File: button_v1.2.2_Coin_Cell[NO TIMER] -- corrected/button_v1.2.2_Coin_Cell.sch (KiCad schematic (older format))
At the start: 20 parts, among them J1 Conn_01x05_Female, SW1 SW_Push, SW2 SW_Push, U1 TPS61097A, X1 ESP-12E

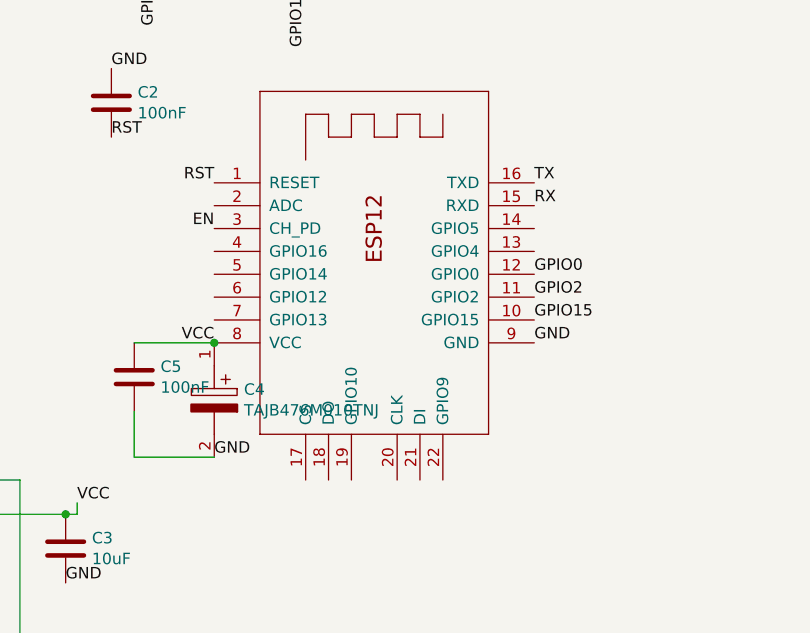
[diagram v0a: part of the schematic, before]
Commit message: All Footprints corrected
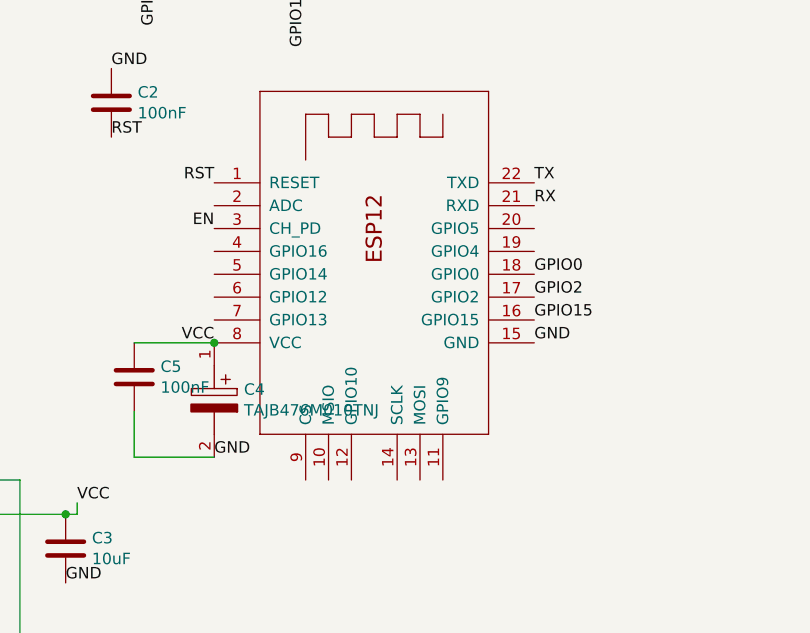
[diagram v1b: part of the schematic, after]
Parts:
- removed X1: ESP-12E, RF_Module:ESP-12E, symbol button_v1.2.2_Coin_Cell-rescue:ESP-12E-ardafruit-button-timer-rescue-button-tim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
- added X1: ESP-12E, handsolder:ESP-12Elesssilk, symbol ardafruit:ESP-12E
- D1: footprint LED_SMD:LED_1206_3216Metric_Castellated -> handsolder:LED_1206_3216Metric_Castellated
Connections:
- net EN: now also X1.3 (CH_PD)
- net GND: now also X1.15 (GND)
- net GPIO0: now also X1.18 (GPIO0)
- net GPIO15: now also X1.16 (GPIO15)
- net GPIO2: now also X1.17 (GPIO2)
- net RST: now also X1.1 (RESET)
- net RX: now also X1.21 (RXD)
- net TX: now also X1.22 (TXD)
- net VCC: now also X1.8 (VCC)
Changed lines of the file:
@@
 F 0 "D1" V 2547 3478 50  0000 L CNN
 F 1 "LED" V 2638 3478 50  0000 L CNN
-F 2 "LED_SMD:LED_1206_3216Metric_Castellated" H 2600 3400 50  0001 C CNN
+F 2 "handsolder:LED_1206_3216Metric_Castellated" H 2600 3400 50  0001 C CNN
 F 3 "~" H 2600 3400 50  0001 C CNN
 	1    2600 3400
@@
 Text Label 6700 3700 0    50   ~ 0
 GND
-$Comp
-L button_v1.2.2_Coin_Cell-rescue:ESP-12E-ardafruit-button-timer-rescue-button-timer-v1.2-rescue-button-timer-v1.2-rescue-button-timer-v1.2.1_Coin_Cell-rescue X1
-U 1 1 602C0443
-P 6000 3400
-F 0 "X1" H 6000 3400 50  0001 C CNN
-F 1 "ESP-12E" H 6000 3400 50  0001 C CNN
-F 2 "RF_Module:ESP-12E" H 6000 3400 50  0001 C CNN
-F 3 "" H 6000 3400 50  0001 C CNN
-	1    6000 3400
-	1    0    0    -1
-$EndComp
 Wire Wire Line
 	3350 5550 4450 5550
@@
 Wire Wire Line
 	4950 3700 5300 3700
+Wire Wire Line
+	4950 4000 4950 4200
+Wire Wire Line
+	4950 4200 5300 4200
+$Comp
+L ardafruit:ESP-12E X1
+U 1 1 603C26C9
+P 6000 3400
+F 0 "X1" H 6000 3400 50  0001 C CNN
+F 1 "ESP-12E" H 6000 3400 50  0001 C CNN
+F 2 "handsolder:ESP-12Elesssilk" H 6000 3400 50  0001 C CNN
+F 3 "" H 6000 3400 50  0001 C CNN
+	1    6000 3400
+	1    0    0    -1
+$EndComp
 Connection ~ 5300 3700
-Wire Wire Line
-	4950 4000 4950 4200
-Wire Wire Line
-	4950 4200 5300 4200
 $EndSCHEMATC
